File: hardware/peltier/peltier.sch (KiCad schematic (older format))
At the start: 33 parts, among them J1 Conn_01x02, J2 Conn_01x04, J3 Conn_01x04, J5 Conn_01x02, J6 Conn_01x03, Q1 IRF9Z34NPBF, Q2 IRF9Z34NPBF, Q3 IRFZ24NPBF, Q4 IRFZ24NPBF, U1 TC4420CPA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

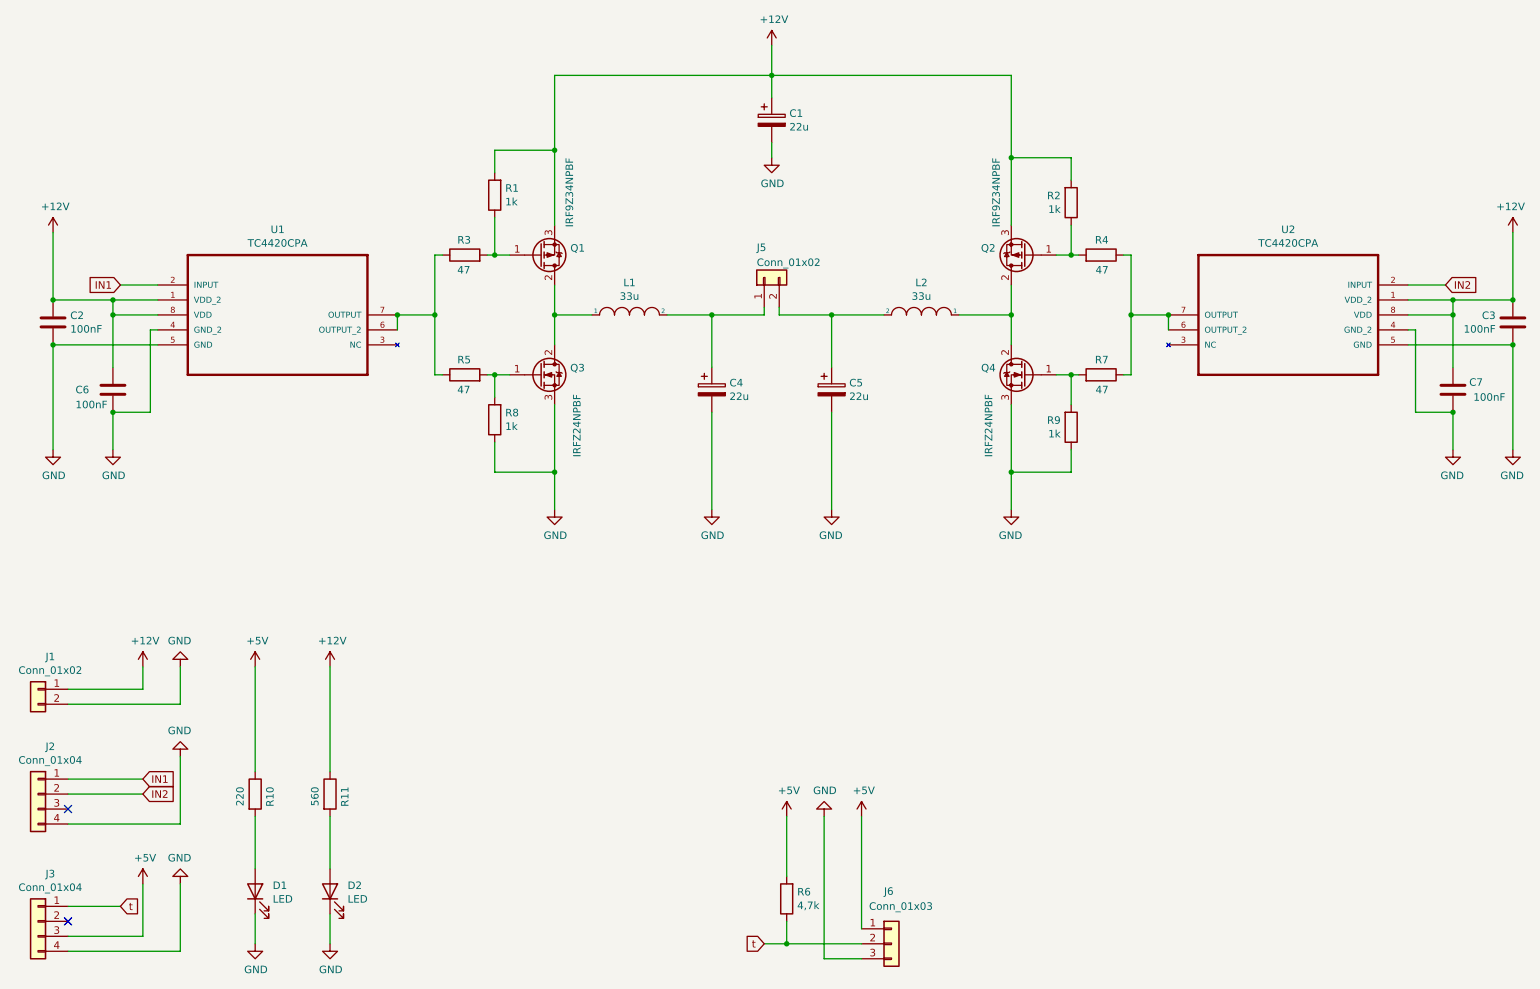
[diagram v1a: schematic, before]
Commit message: Update on 12V5A system power line
- 12V5A power line is now represented by two connectors with 2 pins across all the modules
- all .png previews are updated. The central hub now has previews for schematics, PCB tracing and 3D model
- peltier module now has two 12V5A connectors with redesigned one side of the bridge. Now all MOSFETs can be equipped with heatsinks
- hum/temp sensor now has its connector position reversed to mimic Grove's one
- hum/temp and gas sensors now have a small BeeHive logo on front layer rather than one big on back layer
- hum/temp sensor now use only one layer for signals and one layer for ground
- switch arrays now have two connectors for 12V5A and 5V3A power lines
- switch arrays had their power lines better traced (no sharp turns)
- power supply (12V5A to 5V3A) now has two connectors for 12V5A power line
- one trace of power supply, which lies in between LM2596's legs, was narrowed to ensure that it will not be accidentally soldered or damaged during placement
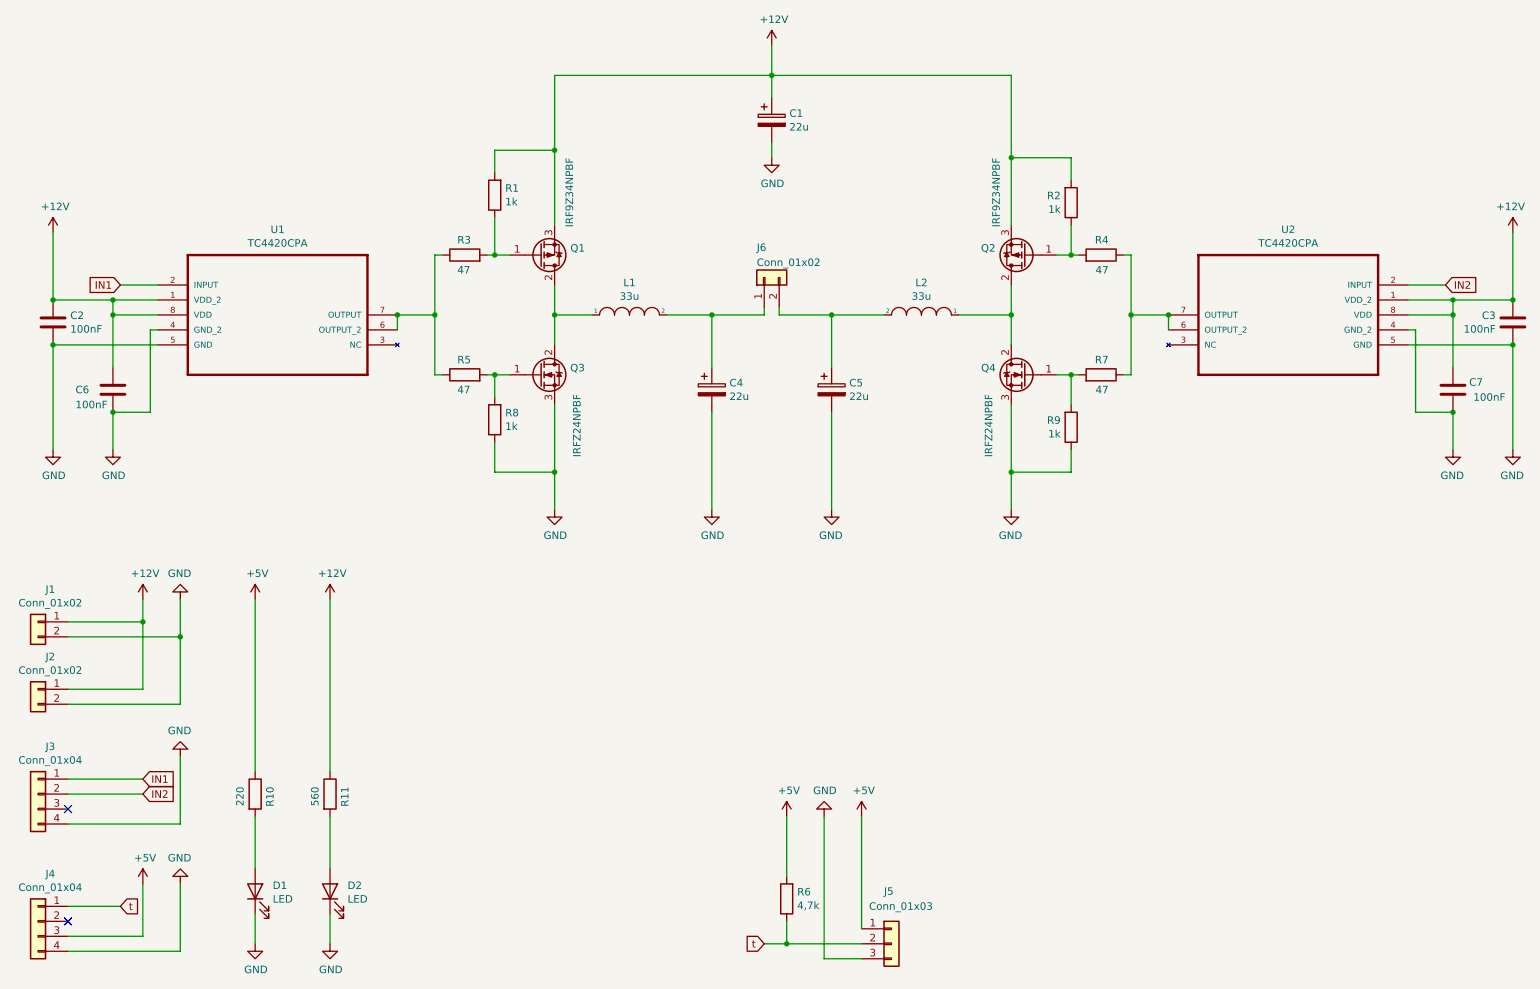
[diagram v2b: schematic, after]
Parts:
- added J1: Conn_01x02, Connector_JST:JST_XH_B2B-XH-A_1x02_P2.50mm_Vertical, symbol Connector_Generic:Conn_01x02
- renumbered J1 to J2, J2 to J3, J3 to J4, J6 to J5, J5 to J6
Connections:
- net +12V: now also J1.1 (Pin_1)
- net GND: now also J1.2 (Pin_2)
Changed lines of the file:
@@
 $EndComp
 $Comp
-L Connector_Generic:Conn_01x02 J5
+L Connector_Generic:Conn_01x02 J6
 U 1 1 5F5966B6
 P 5600 3050
-F 0 "J5" V 5800 3100 50  0000 R CNN
+F 0 "J6" V 5800 3100 50  0000 R CNN
 F 1 "Conn_01x02" V 5700 3100 50  0000 R CNN
 F 2 "Connector_JST:JST_XH_B2B-XH-A_1x02_P2.50mm_Vertical" H 5600 3050 50  0001 C CNN
@@
 	5700 3300 6050 3300
 $Comp
-L Connector_Generic:Conn_01x03 J6
+L Connector_Generic:Conn_01x03 J5
 U 1 1 5F5A1EB6
 P 6450 7500
-F 0 "J6" H 6400 7850 50  0000 L CNN
+F 0 "J5" H 6400 7850 50  0000 L CNN
 F 1 "Conn_01x03" H 6300 7750 50  0000 L CNN
 F 2 "TerminalBlock_TE-Connectivity:TerminalBlock_TE_282834-3_1x03_P2.54mm_Horizontal" H 6450 7500 50  0001 C CNN
@@
 $EndComp
 $Comp
-L Connector_Generic:Conn_01x04 J3
+L Connector_Generic:Conn_01x04 J4
 U 1 1 5F59DECB
 P 750 7350
-F 0 "J3" H 668 7667 50  0000 C CNN
+F 0 "J4" H 668 7667 50  0000 C CNN
 F 1 "Conn_01x04" H 668 7576 50  0000 C CNN
 F 2 "Connector_JST:JST_XH_B4B-XH-A_1x04_P2.50mm_Vertical" H 750 7350 50  0001 C CNN
@@
 	-1   0    0    1
 $EndComp
-$Comp
-L power:GND #PWR01
-U 1 1 5F5E28D2
-P 1700 5650
-F 0 "#PWR01" H 1700 5400 50  0001 C CNN
-F 1 "GND" H 1705 5477 50  0000 C CNN
-F 2 "" H 1700 5650 50  0001 C CNN
-F 3 "" H 1700 5650 50  0001 C CNN
-	1    1700 5650
-	-1   0    0    1
-$EndComp
-$Comp
-L power:+12V #PWR07
-U 1 1 5F5E4300
-P 1450 5650
-F 0 "#PWR07" H 1450 5500 50  0001 C CNN
-F 1 "+12V" H 1465 5823 50  0000 C CNN
-F 2 "" H 1450 5650 50  0001 C CNN
-F 3 "" H 1450 5650 50  0001 C CNN
-	1    1450 5650
-	1    0    0    -1
-$EndComp
-Wire Wire Line
-	1450 5650 1450 5800
 Text GLabel 1450 6500 2    50   Input ~ 0
 IN2
@@
 	2700 7300 2700 7500
 $Comp
-L power:+5V #PWR0103
-U 1 1 5F6BD29C
-P 2200 5650
-F 0 "#PWR0103" H 2200 5500 50  0001 C CNN
-F 1 "+5V" H 2215 5823 50  0000 C CNN
-F 2 "" H 2200 5650 50  0001 C CNN
-F 3 "" H 2200 5650 50  0001 C CNN
-	1    2200 5650
-	1    0    0    -1
-$EndComp
-Wire Wire Line
-	2200 5650 2200 6350
-$Comp
 L power:+12V #PWR0104
 U 1 1 5F6DA569
-P 2700 5650
-F 0 "#PWR0104" H 2700 5500 50  0001 C CNN
-F 1 "+12V" H 2715 5823 50  0000 C CNN
-F 2 "" H 2700 5650 50  0001 C CNN
-F 3 "" H 2700 5650 50  0001 C CNN
-	1    2700 5650
-	1    0    0    -1
-$EndComp
-Wire Wire Line
-	2700 5650 2700 6350
+P 2700 5200
+F 0 "#PWR0104" H 2700 5050 50  0001 C CNN
+F 1 "+12V" H 2715 5373 50  0000 C CNN
+F 2 "" H 2700 5200 50  0001 C CNN
+F 3 "" H 2700 5200 50  0001 C CNN
+	1    2700 5200
+	1    0    0    -1
+$EndComp
+Wire Wire Line
+	2700 5200 2700 6350
 Connection ~ 3400 3300
 Wire Wire Line
@@
 $EndComp
 $Comp
-L Connector_Generic:Conn_01x04 J2
+L Connector_Generic:Conn_01x04 J3
 U 1 1 5F58D029
 P 750 6500
-F 0 "J2" H 668 6817 50  0000 C CNN
+F 0 "J3" H 668 6817 50  0000 C CNN
 F 1 "Conn_01x04" H 668 6726 50  0000 C CNN
 F 2 "Connector_JST:JST_XH_B4B-XH-A_1x04_P2.50mm_Vertical" H 750 6500 50  0001 C CNN
@@
 $EndComp
 Wire Wire Line
-	1700 5650 1700 5900
-Wire Wire Line
-	950  5800 1450 5800
-Wire Wire Line
-	950  5900 1700 5900
+	950  6500 1450 6500
+Wire Wire Line
+	950  6700 1700 6700
+Wire Wire Line
+	1700 6250 1700 6700
+NoConn ~ 950  6600
+Wire Wire Line
+	950  7450 1450 7450
+Wire Wire Line
+	1450 7100 1450 7450
+Wire Wire Line
+	1300 7250 950  7250
+Wire Wire Line
+	1700 7100 1700 7550
+Wire Wire Line
+	950  7550 1700 7550
+NoConn ~ 950  7350
+Wire Wire Line
+	1700 5450 1700 5900
+Connection ~ 1700 5450
+Wire Wire Line
+	950  5450 1700 5450
+Wire Wire Line
+	1450 5350 1450 5800
+Connection ~ 1450 5350
+Wire Wire Line
+	950  5350 1450 5350
+Wire Wire Line
+	1700 5200 1700 5450
+Wire Wire Line
+	1450 5200 1450 5350
 $Comp
 L Connector_Generic:Conn_01x02 J1
+U 1 1 5FD289CF
+P 750 5350
+F 0 "J1" H 668 5567 50  0000 C CNN
+F 1 "Conn_01x02" H 668 5476 50  0000 C CNN
+F 2 "Connector_JST:JST_XH_B2B-XH-A_1x02_P2.50mm_Vertical" H 750 5350 50  0001 C CNN
+F 3 "~" H 750 5350 50  0001 C CNN
+	1    750  5350
+	-1   0    0    -1
+$EndComp
+$Comp
+L Connector_Generic:Conn_01x02 J2
 U 1 1 5F5E0D51
 P 750 5800
-F 0 "J1" H 668 6017 50  0000 C CNN
+F 0 "J2" H 668 6017 50  0000 C CNN
 F 1 "Conn_01x02" H 668 5926 50  0000 C CNN
 F 2 "Connector_JST:JST_XH_B2B-XH-A_1x02_P2.50mm_Vertical" H 750 5800 50  0001 C CNN
@@
 $EndComp
 Wire Wire Line
-	950  6500 1450 6500
-Wire Wire Line
-	950  6700 1700 6700
-Wire Wire Line
-	1700 6250 1700 6700
-NoConn ~ 950  6600
-Wire Wire Line
-	950  7450 1450 7450
-Wire Wire Line
-	1450 7100 1450 7450
-Wire Wire Line
-	1300 7250 950  7250
-Wire Wire Line
-	1700 7100 1700 7550
-Wire Wire Line
-	950  7550 1700 7550
-NoConn ~ 950  7350
+	950  5900 1700 5900
+Wire Wire Line
+	950  5800 1450 5800
+Wire Wire Line
+	2200 5200 2200 6350
+$Comp
+L power:+5V #PWR0103
+U 1 1 5F6BD29C
+P 2200 5200
+F 0 "#PWR0103" H 2200 5050 50  0001 C CNN
+F 1 "+5V" H 2215 5373 50  0000 C CNN
+F 2 "" H 2200 5200 50  0001 C CNN
+F 3 "" H 2200 5200 50  0001 C CNN
+	1    2200 5200
+	1    0    0    -1
+$EndComp
+$Comp
+L power:+12V #PWR07
+U 1 1 5F5E4300
+P 1450 5200
+F 0 "#PWR07" H 1450 5050 50  0001 C CNN
+F 1 "+12V" H 1465 5373 50  0000 C CNN
+F 2 "" H 1450 5200 50  0001 C CNN
+F 3 "" H 1450 5200 50  0001 C CNN
+	1    1450 5200
+	1    0    0    -1
+$EndComp
+$Comp
+L power:GND #PWR01
+U 1 1 5F5E28D2
+P 1700 5200
+F 0 "#PWR01" H 1700 4950 50  0001 C CNN
+F 1 "GND" H 1705 5027 50  0000 C CNN
+F 2 "" H 1700 5200 50  0001 C CNN
+F 3 "" H 1700 5200 50  0001 C CNN
+	1    1700 5200
+	-1   0    0    1
+$EndComp
 $EndSCHEMATC
